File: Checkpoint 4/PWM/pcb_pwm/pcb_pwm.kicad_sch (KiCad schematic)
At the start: 29 parts, among them J2 Conn_01x03_Socket, J3 Conn_01x06_Socket, U1 TL082, U2 LM2901

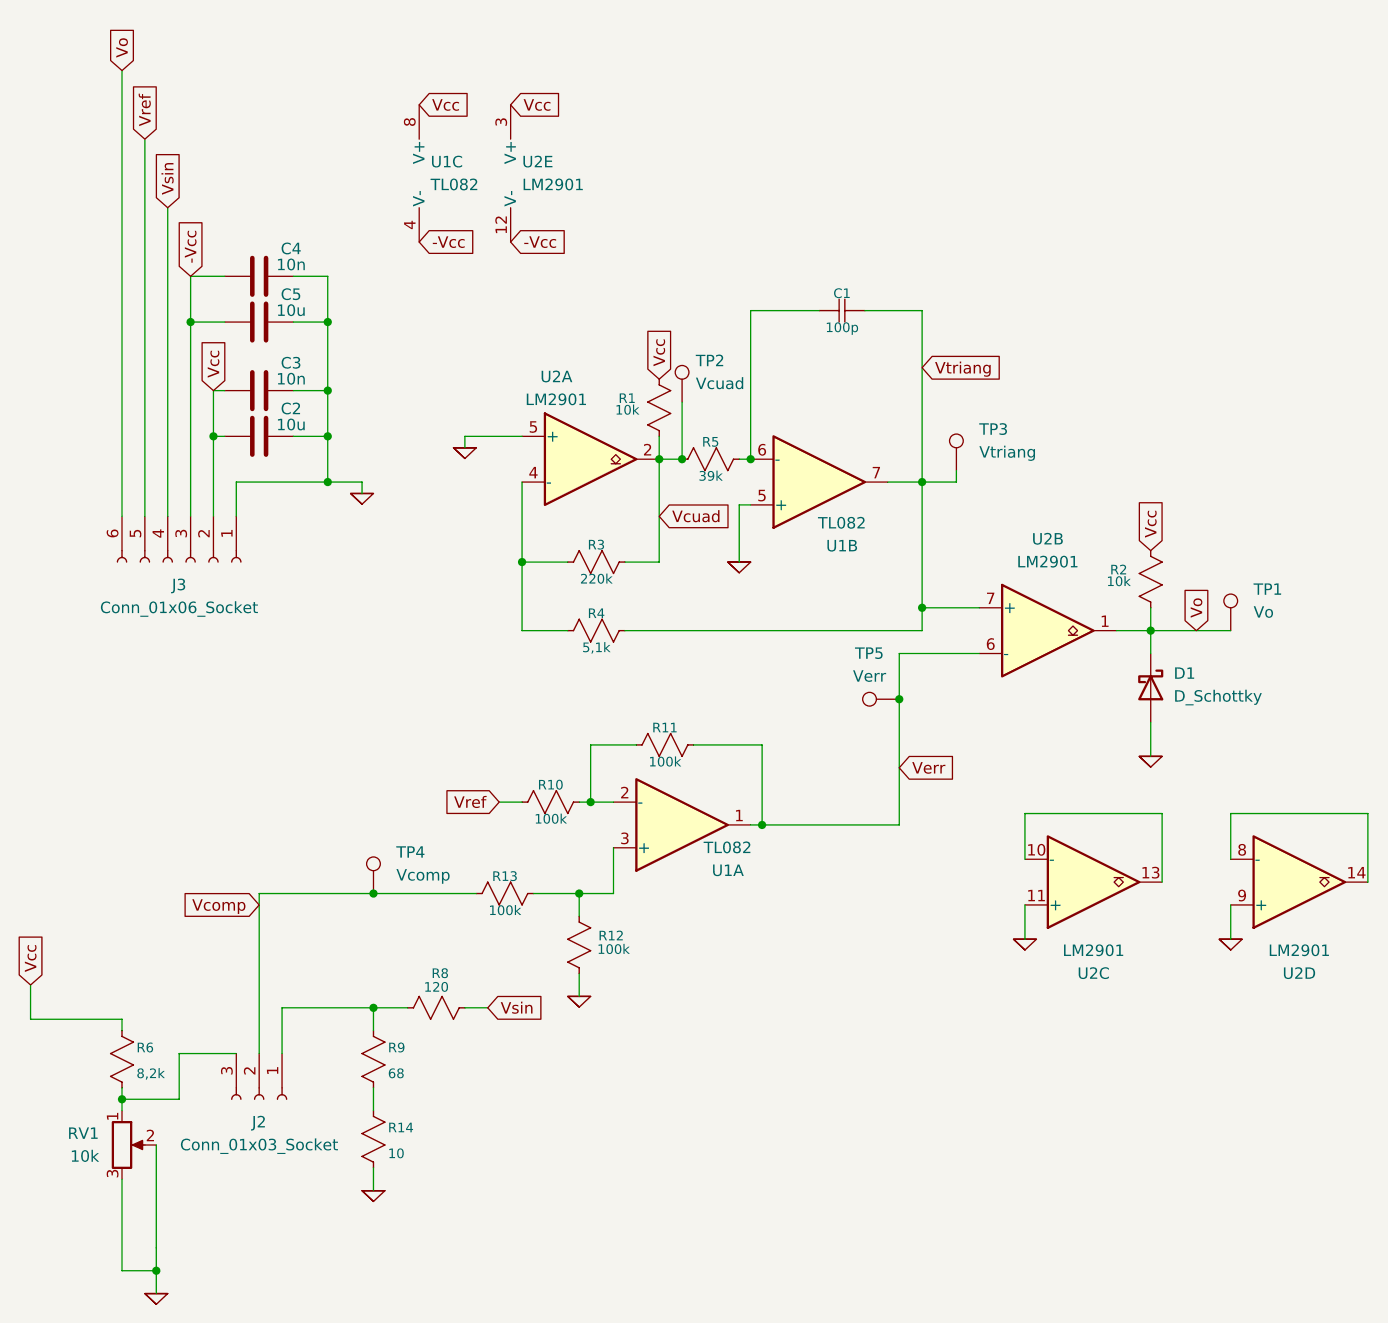
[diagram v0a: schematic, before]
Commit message: sube cambios en el pcb del pwm, y cambios pruebas en la simu del buck
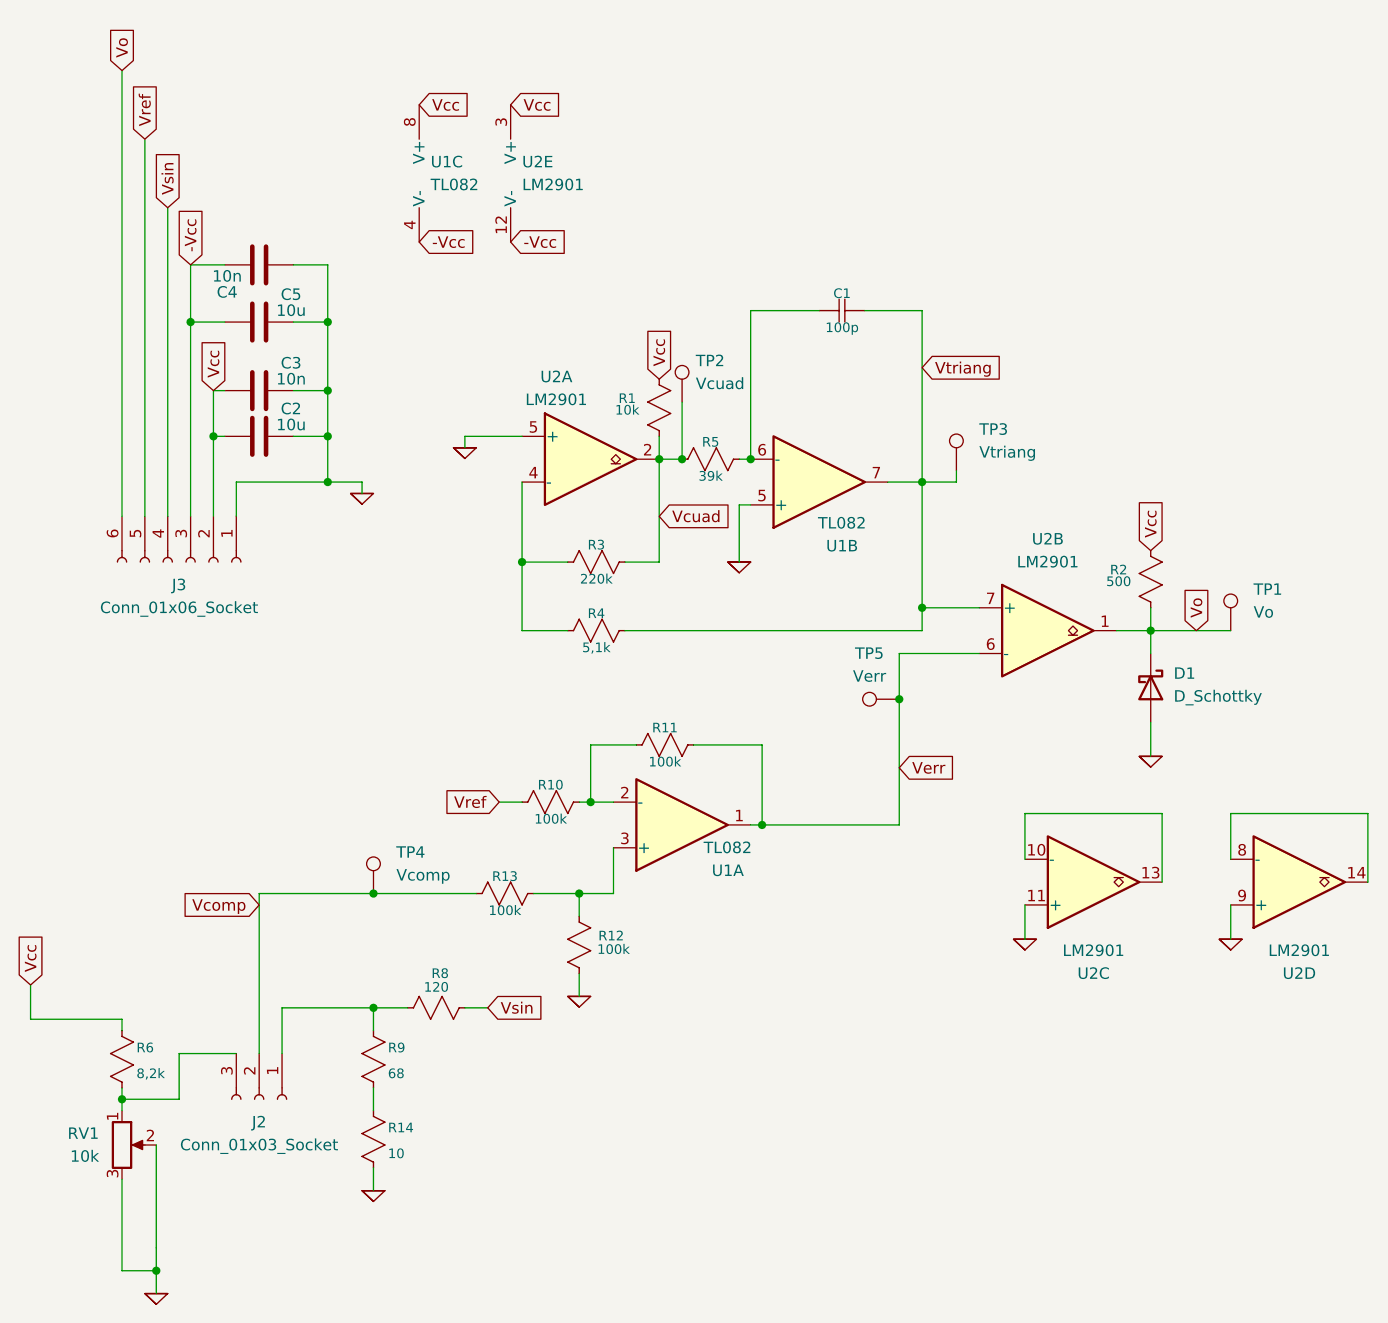
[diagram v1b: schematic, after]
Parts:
- D1: footprint Diode_THT:D_DO-27_P12.70mm_Horizontal -> Package_TO_SOT_THT:TO-220-2_Vertical
- R2: value 10k -> 500
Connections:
- net -Vcc: now also C4.2; no longer C4.1
- net 0: now also C4.1; no longer C4.2
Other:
- moved on the sheet: C4
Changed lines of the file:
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@@
 	(wire
 		(pts
-			(xy 85.09 64.77) (xy 88.9 64.77)
+			(xy 85.09 63.5) (xy 88.9 63.5)
 		)
 		(stroke
@@
 	(wire
 		(pts
-			(xy 73.66 64.77) (xy 73.66 69.85)
+			(xy 73.66 63.5) (xy 73.66 69.85)
 		)
 		(stroke
@@
 	(wire
 		(pts
-			(xy 73.66 64.77) (xy 77.47 64.77)
+			(xy 73.66 63.5) (xy 77.47 63.5)
 		)
 		(stroke
@@
 	(wire
 		(pts
-			(xy 88.9 64.77) (xy 88.9 69.85)
+			(xy 88.9 63.5) (xy 88.9 69.85)
 		)
 		(stroke
@@
 	(global_label "-Vcc"
 		(shape input)
-		(at 73.66 64.77 90)
+		(at 73.66 63.5 90)
 		(fields_autoplaced yes)
 		(effects
@@
 		)
 		(property "Intersheetrefs" "${INTERSHEET_REFS}"
-			(at 73.66 56.9466 90)
+			(at 73.66 55.6766 90)
 			(effects
 				(font
@@
 			)
 		)
-		(property "Value" "10k"
+		(property "Value" "500"
 			(at 176.784 99.314 0)
 			(effects
@@
 	(symbol
 		(lib_id "Device:C")
-		(at 81.28 64.77 90)
+		(at 81.28 63.5 270)
 		(unit 1)
 		(exclude_from_sim no)
@@
 		(dnp no)
 		(property "Reference" "C4"
-			(at 84.836 61.722 90)
+			(at 77.724 66.548 90)
 			(effects
 				(font
@@
 		)
 		(property "Value" "10n"
-			(at 84.836 63.5 90)
+			(at 77.724 64.77 90)
 			(effects
 				(font
@@
 		)
 		(property "Footprint" "Capacitor_THT:C_Disc_D3.4mm_W2.1mm_P2.50mm"
-			(at 85.09 63.8048 0)
+			(at 77.47 64.4652 0)
 			(effects
 				(font
@@
 		)
 		(property "Datasheet" "~"
-			(at 81.28 64.77 0)
+			(at 81.28 63.5 0)
 			(effects
 				(font
@@
 		)
 		(property "Description" "Unpolarized capacitor"
-			(at 81.28 64.77 0)
+			(at 81.28 63.5 0)
 			(effects
 				(font
@@
 			)
 		)
-		(property "Footprint" "Diode_THT:D_DO-27_P12.70mm_Horizontal"
+		(property "Footprint" "Package_TO_SOT_THT:TO-220-2_Vertical"
 			(at 180.34 110.49 0)
 			(effects

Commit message: pcb pwm y buck final
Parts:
- C3, C4: footprint Capacitor_THT:C_Disc_D3.4mm_W2.1mm_P2.50mm -> Capacitor_THT:C_Disc_D4.3mm_W1.9mm_P5.00mm
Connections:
- net Vo: no longer J3.6 (Pin_6)
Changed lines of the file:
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@@
-		)
-	)
-	(global_label "Vo"
-		(shape input)
-		(at 66.04 41.91 90)
-		(fields_autoplaced yes)
-		(effects
-			(font
-				(size 1.27 1.27)
-			)
-			(justify left)
-		)
-		(property "Intersheetrefs" "${INTERSHEET_REFS}"
-			(at 66.04 36.6872 90)
-			(effects
-				(font
-					(size 1.27 1.27)
-				)
-				(justify left)
-				(hide yes)
-			)
 		)
 	)
@@
 			)
 		)
-		(property "Footprint" "Capacitor_THT:C_Disc_D3.4mm_W2.1mm_P2.50mm"
+		(property "Footprint" "Capacitor_THT:C_Disc_D4.3mm_W1.9mm_P5.00mm"
 			(at 85.09 76.5048 0)
 			(effects
@@
 			)
 		)
-		(property "Footprint" "Capacitor_THT:C_Disc_D3.4mm_W2.1mm_P2.50mm"
+		(property "Footprint" "Capacitor_THT:C_Disc_D4.3mm_W1.9mm_P5.00mm"
 			(at 77.47 64.4652 0)
 			(effects

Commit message: a ver si ahora si funcan los pcb sino me mato
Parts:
- R10, R11, R12, R13: value 100k -> 390k
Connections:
- net 0: now also U2.4 (-); no longer U2.5 (+)
- net at R3.2, R4.2: now also U2.5 (+); no longer U2.4 (-)
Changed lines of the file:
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@@
 			)
 		)
-		(property "Value" "100k"
+		(property "Value" "390k"
 			(at 113.665 124.46 90)
 			(effects
@@
 			)
 		)
-		(property "Value" "100k"
+		(property "Value" "390k"
 			(at 108.585 134.62 90)
 			(effects
@@
 		(lib_id "Comparator:LM2901")
 		(at 118.11 85.09 0)
+		(mirror x)
 		(unit 1)
 		(exclude_from_sim no)
@@
 		(dnp no)
 		(property "Reference" "U2"
-			(at 114.3 75.946 0)
+			(at 114.554 78.232 0)
 			(effects
 				(font
@@
 		)
 		(property "Value" "LM2901"
-			(at 114.3 78.486 0)
+			(at 114.554 75.692 0)
 			(effects
 				(font
@@
 		)
 		(property "Footprint" "Package_DIP:DIP-14_W7.62mm_Socket"
-			(at 116.84 82.55 0)
+			(at 116.84 87.63 0)
 			(effects
 				(font
@@
 		)
 		(property "Datasheet" "https://www.st.com/resource/en/datasheet/lm2901.pdf"
-			(at 119.38 80.01 0)
+			(at 119.38 90.17 0)
 			(effects
 				(font
@@
 			)
 		)
-		(property "Value" "100k"
+		(property "Value" "390k"
 			(at 126.365 118.11 90)
 			(effects
@@
 			)
 		)
-		(property "Value" "100k"
+		(property "Value" "390k"
 			(at 120.65 138.938 0)
 			(effects
